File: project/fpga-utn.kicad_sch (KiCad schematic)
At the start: 0 parts

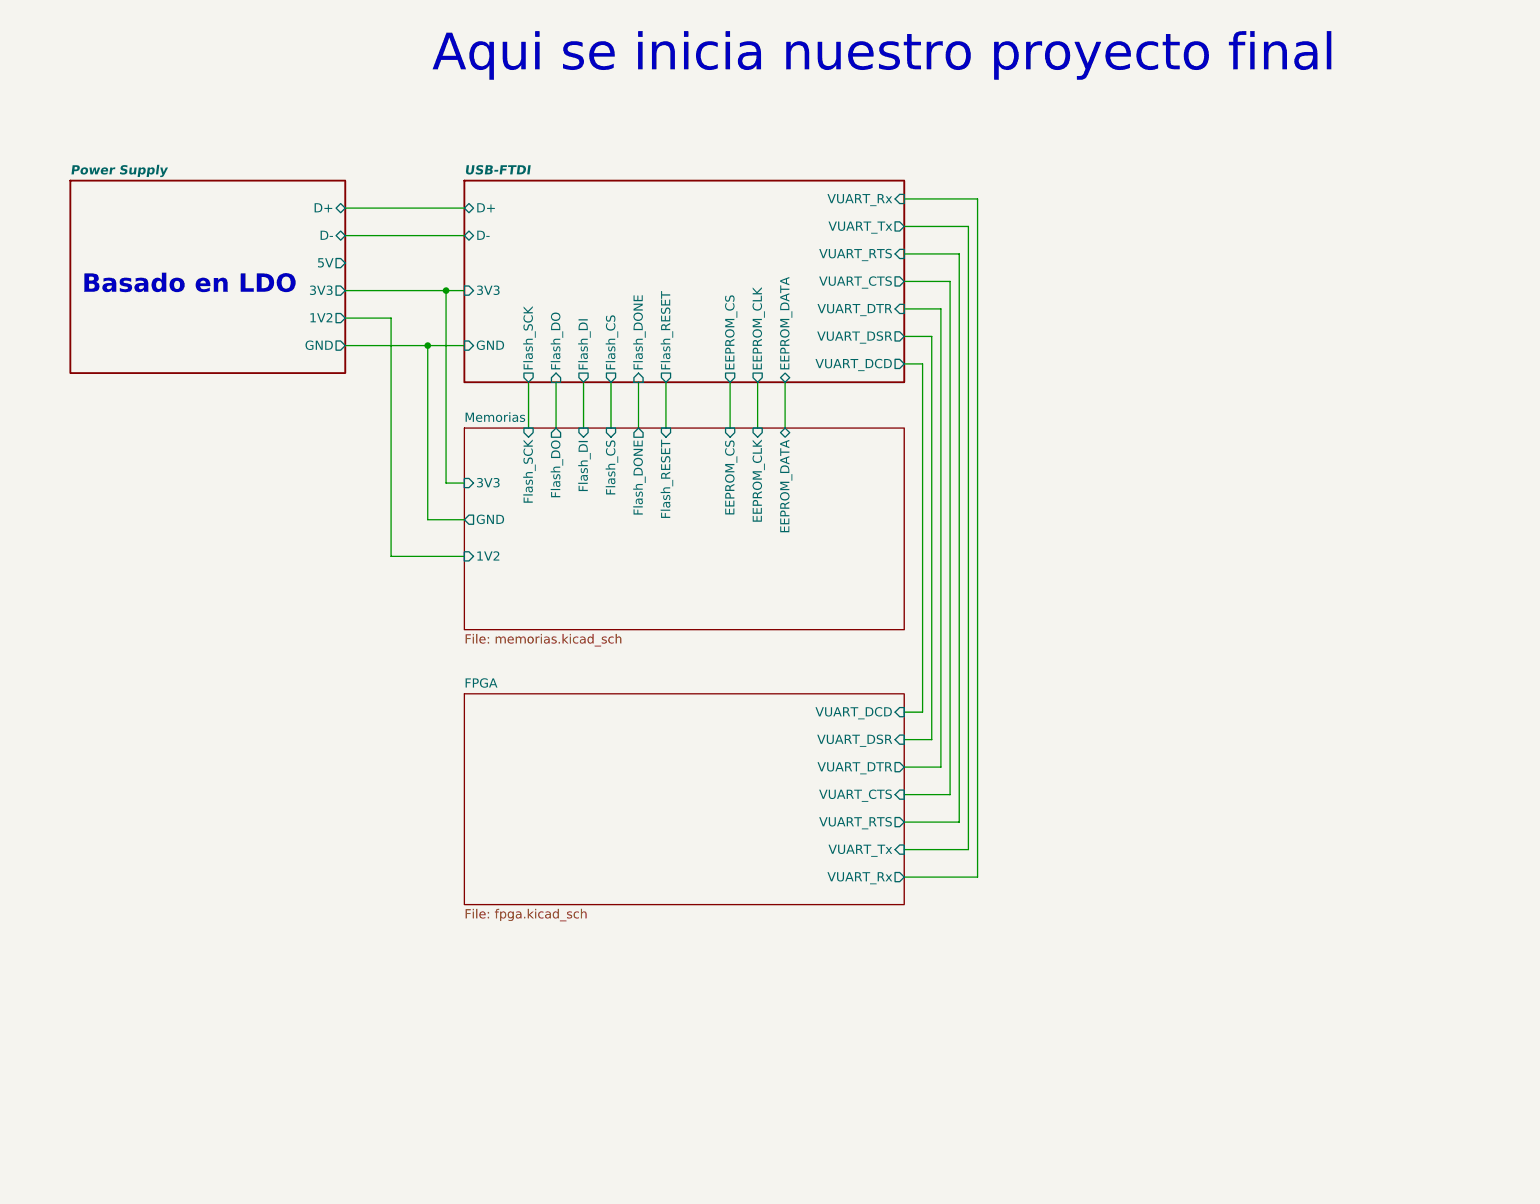
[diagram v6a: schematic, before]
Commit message: Eliminación de archivos de respaldo y correcciones en la biblioteca de componentes. Se eliminaron archivos de autosave, archivos de esquemas y modelos 3D no utilizados, así como modificaciones en las propiedades de algunos componentes en la biblioteca.
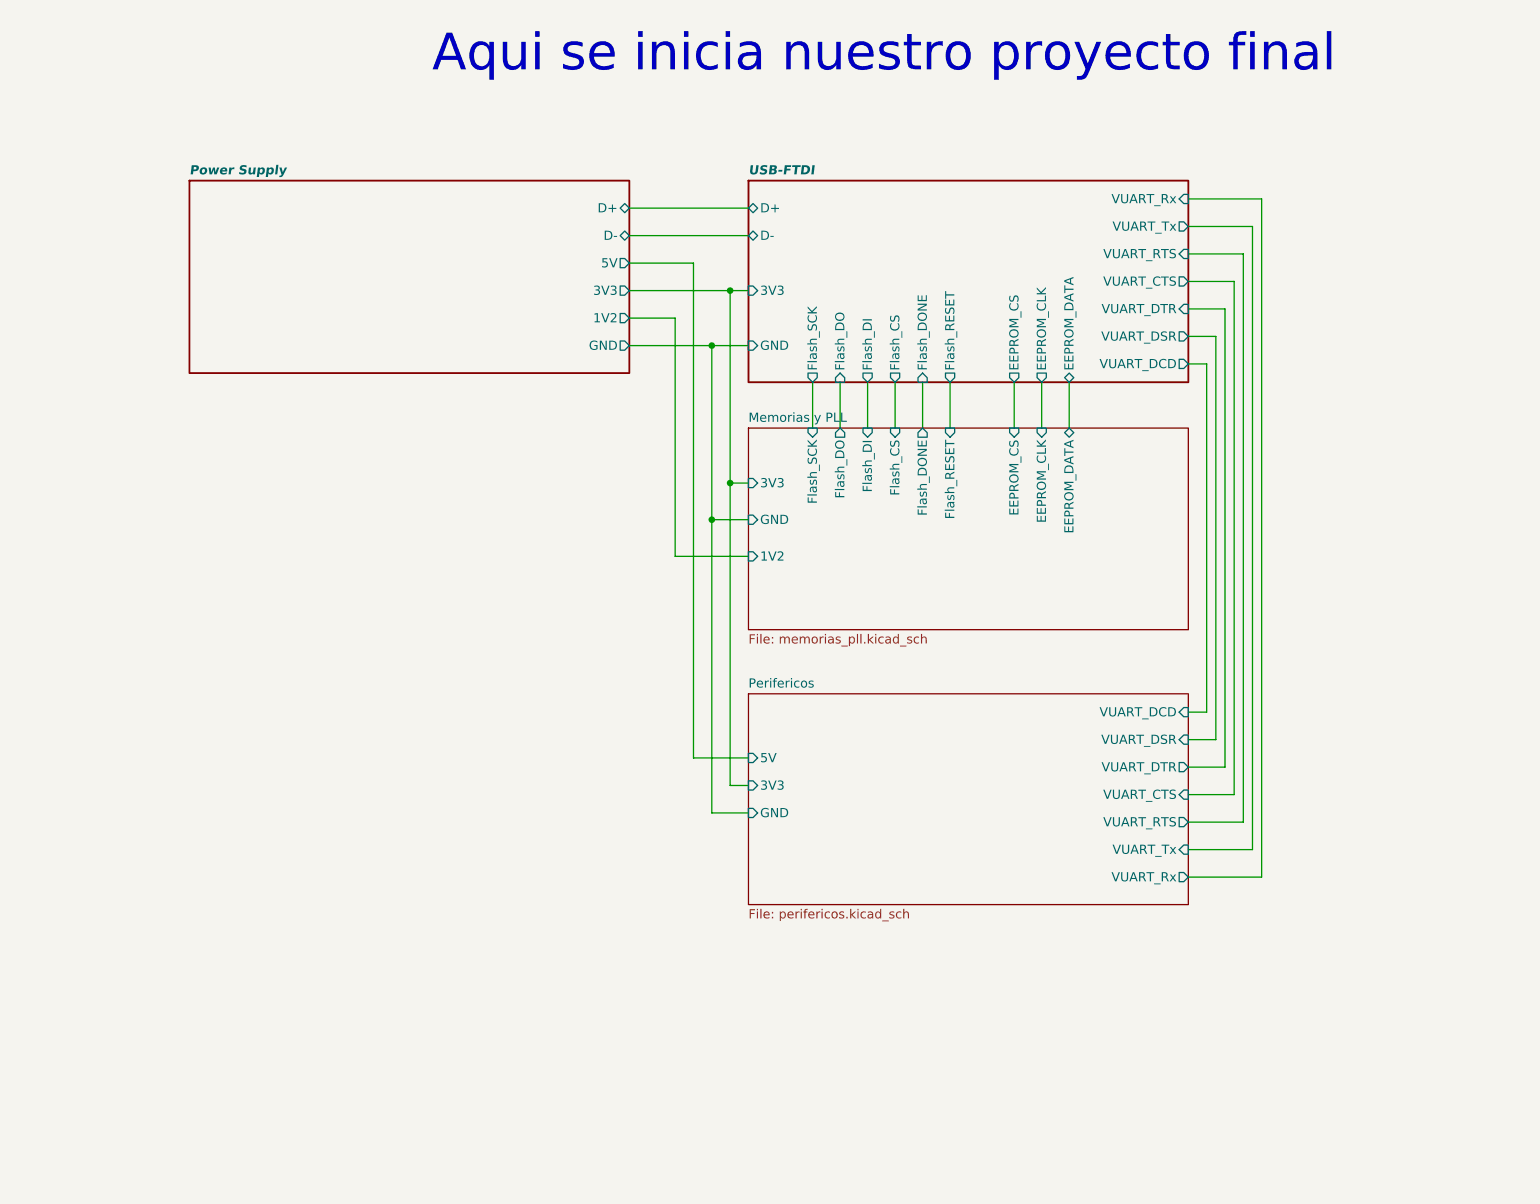
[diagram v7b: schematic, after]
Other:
- sheet FPGA renamed Perifericos
- sheet Memorias renamed Memorias y PLL
- sheet Memorias y PLL: file memorias.kicad_sch -> memorias_pll.kicad_sch
- sheet Perifericos: file fpga.kicad_sch -> perifericos.kicad_sch
- sheet Perifericos ports: added 3V3, 5V, GND; removed none
- note removed: "Basado en LDO"

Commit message: Agregado TODO para futuro. Agregado clock de 12 MHz a la FPGA. Agregado pinout de conector 2x10.
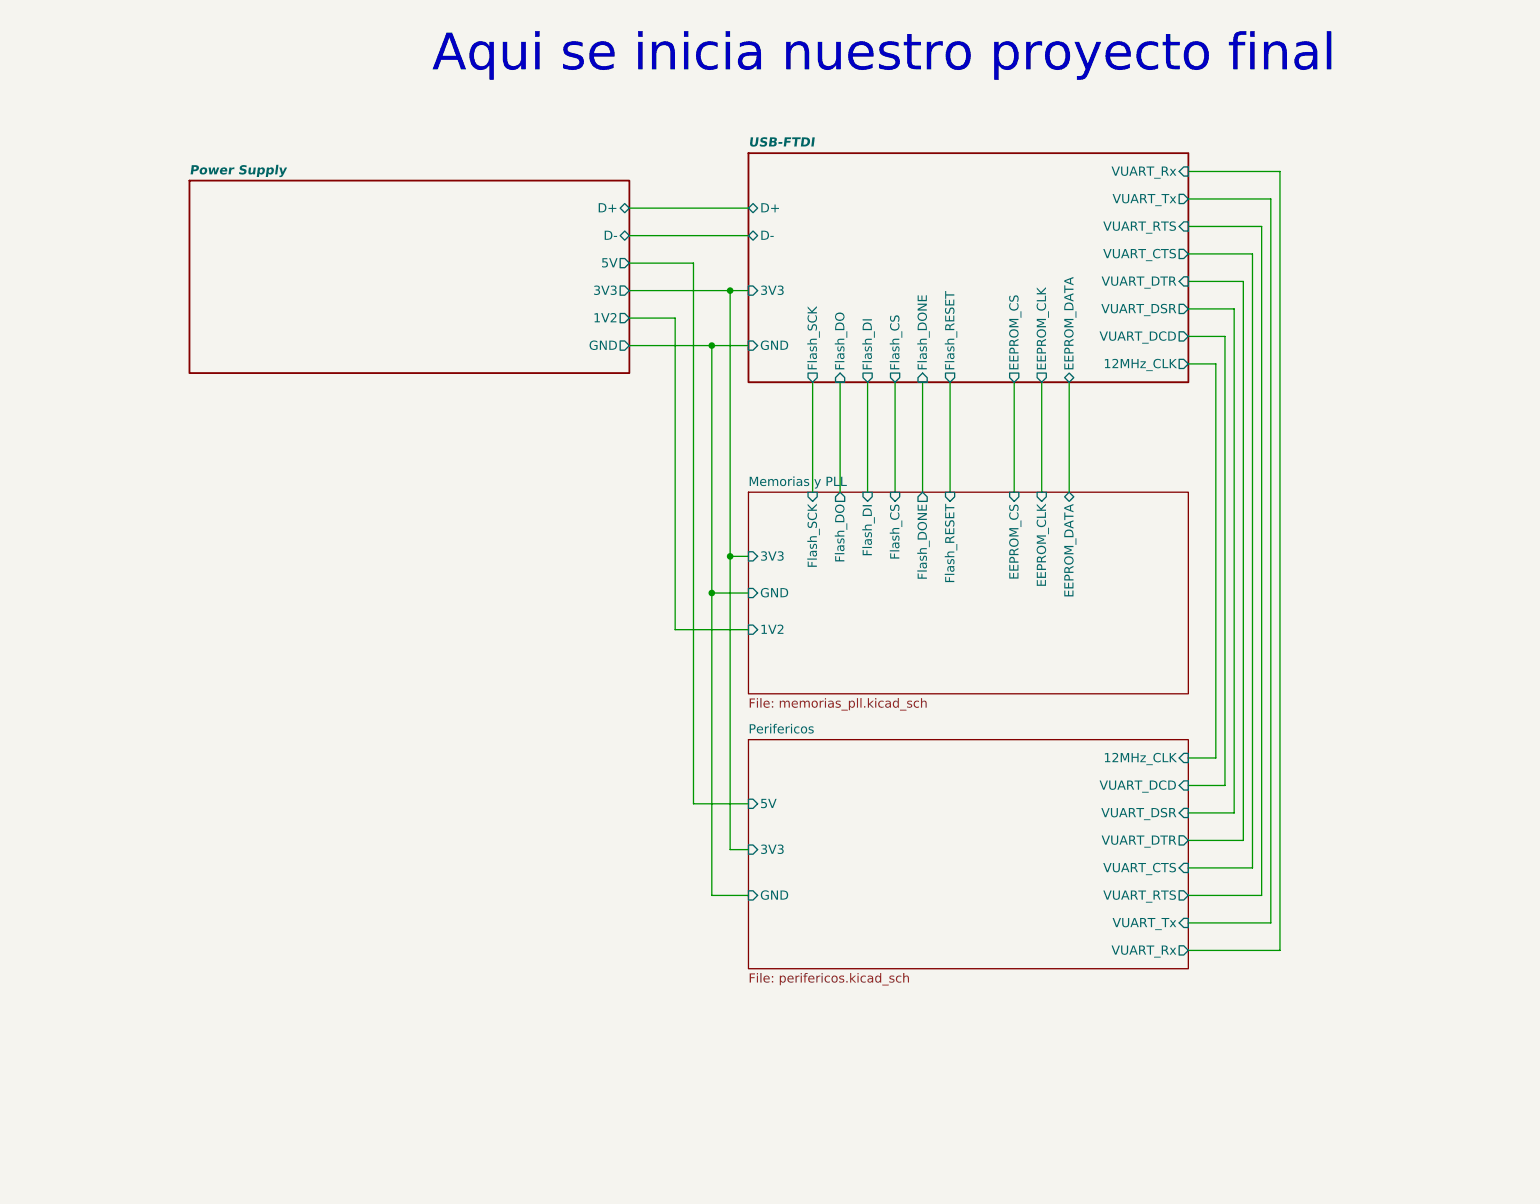
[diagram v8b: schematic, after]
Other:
- sheet Perifericos ports: added 12MHz_CLK; removed none
- sheet USB-FTDI ports: added 12MHz_CLK; removed none
